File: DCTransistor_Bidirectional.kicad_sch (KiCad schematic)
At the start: 277 parts, among them J0 USB_C_Receptacle, Q0 MMBT3904, Q1 MMBT3904, Q2 AOD403, U0 CH340C, U2 ESP-12F, U3 SN74LVC1T45DBV, U4 TLV70233DBVR

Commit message: layout and footprint changes
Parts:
- removed SYMBOL0, SYMBOL1: ~, Jarrett_Footprint_Library:Trans_Symbol, symbol Jannett_Symbol_Library:Trans_Symbol
- removed SYMBOL2: ~, Jarrett_Footprint_Library:DCTransistor-Adjusted_Stations, symbol Jannett_Symbol_Library:Trans_Symbol
- added C48, C49: 0.1uF, Capacitor_SMD:C_0603_1608Metric, symbol Device:C_Small
- added H0, H1, H2, H3: MountingHole, MountingHole:MountingHole_6.4mm_M6, symbol Mechanical:MountingHole
- added TP0, TP1: 5016, jannett_footprints:TestPoint_Keystone_5016_Compact, symbol Connector:TestPoint
- D10, D100, D101, D102, D103, D104, D105, D106, D107, D108, D109, D11, D110, D111, D112, D113, D114, D115, D116, D117, D118, D119, D12, D120, D121, D122, D123, D124, D125, D126, D127, D128, D129, D13, D130, D131, D132, D133, D134, D135, D136, D137, D138, D139, D14, D140, D141, D142, D143, D144, D145, D146, D147, D148, D149, D15, D150, D151, D152, D153, D154, D155, D156, D157, D158, D159, D16, D160, D161, D162, D163, D164, D165, D166, D167, D168, D169, D17, D170, D171, D172, D173, D174, D175, D176, D177, D178, D179, D18, D180, D181, D182, D183, D184, D185, D186, D187, D188, D189, D19, D190, D191, D192, D193, D194, D195, D196, D197, D198, D199, D2, D20, D200, D201, D202, D203, D204, D205, D206, D207, D208, D21, D22, D23, D24, D25, D26, D27, D28, D29, D3, D30, D31, D32, D33, D34, D35, D36, D37, D38, D39, D4, D40, D41, D42, D43, D44, D45, D46, D47, D48, D49, D5, D50, D51, D52, D53, D54, D55, D56, D57, D58, D59, D6, D60, D61, D62, D63, D64, D65, D66, D67, D68, D69, D7, D70, D71, D72, D73, D74, D75, D76, D77, D78, D79, D8, D80, D81, D82, D83, D84, D85, D86, D87, D88, D89, D9, D90, D91, D92, D93, D94, D95, D96, D97, D98, D99: value WS2812B -> SKC6812RV; footprint LED_SMD:LED_WS2812B_PLCC4_5.0x5.0mm_P3.2mm -> jannett_footprints:LED_SK6812_PLCC4_5.0x5.0mm_P3.2mm_no_silk; symbol LED:WS2812B_2020_pinout -> LED:SK6812
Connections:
- net +3V3: now also C49.2
- net +5V: now also D10.3 (VDD), D100.3 (VDD), D101.3 (VDD), D102.3 (VDD), D103.3 (VDD), D104.3 (VDD), D105.3 (VDD), D106.3 (VDD), D107.3 (VDD), D108.3 (VDD), D109.3 (VDD), D11.3 (VDD), D110.3 (VDD), D111.3 (VDD), D112.3 (VDD), D113.3 (VDD), D114.3 (VDD), D115.3 (VDD), D116.3 (VDD), D117.3 (VDD), D118.3 (VDD), D119.3 (VDD), D12.3 (VDD), D120.3 (VDD), D121.3 (VDD), D122.3 (VDD), D123.3 (VDD), D124.3 (VDD), D125.3 (VDD), D126.3 (VDD), D127.3 (VDD), D128.3 (VDD), D129.3 (VDD), D13.3 (VDD), D130.3 (VDD), D131.3 (VDD), D132.3 (VDD), D133.3 (VDD), D134.3 (VDD), D135.3 (VDD), D136.3 (VDD), D137.3 (VDD), D138.3 (VDD), D139.3 (VDD), D14.3 (VDD), D140.3 (VDD), D141.3 (VDD), D142.3 (VDD), D143.3 (VDD), D144.3 (VDD), D145.3 (VDD), D146.3 (VDD), D147.3 (VDD), D148.3 (VDD), D149.3 (VDD), D15.3 (VDD), D150.3 (VDD), D151.3 (VDD), D152.3 (VDD), D153.3 (VDD), D154.3 (VDD), D155.3 (VDD), D156.3 (VDD), D157.3 (VDD), D158.3 (VDD), D159.3 (VDD), D16.3 (VDD), D160.3 (VDD), D161.3 (VDD), D162.3 (VDD), D163.3 (VDD), D164.3 (VDD), D165.3 (VDD), D166.3 (VDD), D167.3 (VDD), D168.3 (VDD), D169.3 (VDD), D17.3 (VDD), D170.3 (VDD), D171.3 (VDD), D172.3 (VDD), D173.3 (VDD), D174.3 (VDD), D175.3 (VDD), D176.3 (VDD), D177.3 (VDD), D178.3 (VDD), D179.3 (VDD), D18.3 (VDD), D180.3 (VDD), D181.3 (VDD), D182.3 (VDD), D183.3 (VDD), D184.3 (VDD), D185.3 (VDD), D186.3 (VDD), D187.3 (VDD), D188.3 (VDD), D189.3 (VDD), D19.3 (VDD), D190.3 (VDD), D191.3 (VDD), D192.3 (VDD), D193.3 (VDD), D194.3 (VDD), D195.3 (VDD), D196.3 (VDD), D197.3 (VDD), D198.3 (VDD), D199.3 (VDD), D2.3 (VDD), D20.3 (VDD), D200.3 (VDD), D201.3 (VDD), D202.3 (VDD), D203.3 (VDD), D204.3 (VDD), D205.3 (VDD), D206.3 (VDD), D207.3 (VDD), D208.3 (VDD), D21.3 (VDD), D22.3 (VDD), D23.3 (VDD), D24.3 (VDD), D25.3 (VDD), D26.3 (VDD), D27.3 (VDD), D28.3 (VDD), D29.3 (VDD), D3.3 (VDD), D30.3 (VDD), D31.3 (VDD), D32.3 (VDD), D33.3 (VDD), D34.3 (VDD), D35.3 (VDD), D36.3 (VDD), D37.3 (VDD), D38.3 (VDD), D39.3 (VDD), D4.3 (VDD), D40.3 (VDD), D41.3 (VDD), D42.3 (VDD), D43.3 (VDD), D44.3 (VDD), D45.3 (VDD), D46.3 (VDD), D47.3 (VDD), D48.3 (VDD), D49.3 (VDD), D5.3 (VDD), D50.3 (VDD), D51.3 (VDD), D52.3 (VDD), D53.3 (VDD), D54.3 (VDD), D55.3 (VDD), D56.3 (VDD), D57.3 (VDD), D58.3 (VDD), D59.3 (VDD), D6.3 (VDD), D60.3 (VDD), D61.3 (VDD), D62.3 (VDD), D63.3 (VDD), D64.3 (VDD), D65.3 (VDD), D66.3 (VDD), D67.3 (VDD), D68.3 (VDD), D69.3 (VDD), D7.3 (VDD), D70.3 (VDD), D71.3 (VDD), D72.3 (VDD), D73.3 (VDD), D74.3 (VDD), D75.3 (VDD), D76.3 (VDD), D77.3 (VDD), D78.3 (VDD), D79.3 (VDD), D8.3 (VDD), D80.3 (VDD), D81.3 (VDD), D82.3 (VDD), D83.3 (VDD), D84.3 (VDD), D85.3 (VDD), D86.3 (VDD), D87.3 (VDD), D88.3 (VDD), D89.3 (VDD), D9.3 (VDD), D90.3 (VDD), D91.3 (VDD), D92.3 (VDD), D93.3 (VDD), D94.3 (VDD), D95.3 (VDD), D96.3 (VDD), D97.3 (VDD), D98.3 (VDD), D99.3 (VDD), C48.1, TP0.1; no longer D10.4 (VDD), D100.4 (VDD), D101.4 (VDD), D102.4 (VDD), D103.4 (VDD), D104.4 (VDD), D105.4 (VDD), D106.4 (VDD), D107.4 (VDD), D108.4 (VDD), D109.4 (VDD), D11.4 (VDD), D110.4 (VDD), D111.4 (VDD), D112.4 (VDD), D113.4 (VDD), D114.4 (VDD), D115.4 (VDD), D116.4 (VDD), D117.4 (VDD), D118.4 (VDD), D119.4 (VDD), D12.4 (VDD), D120.4 (VDD), D121.4 (VDD), D122.4 (VDD), D123.4 (VDD), D124.4 (VDD), D125.4 (VDD), D126.4 (VDD), D127.4 (VDD), D128.4 (VDD), D129.4 (VDD), D13.4 (VDD), D130.4 (VDD), D131.4 (VDD), D132.4 (VDD), D133.4 (VDD), D134.4 (VDD), D135.4 (VDD), D136.4 (VDD), D137.4 (VDD), D138.4 (VDD), D139.4 (VDD), D14.4 (VDD), D140.4 (VDD), D141.4 (VDD), D142.4 (VDD), D143.4 (VDD), D144.4 (VDD), D145.4 (VDD), D146.4 (VDD), D147.4 (VDD), D148.4 (VDD), D149.4 (VDD), D15.4 (VDD), D150.4 (VDD), D151.4 (VDD), D152.4 (VDD), D153.4 (VDD), D154.4 (VDD), D155.4 (VDD), D156.4 (VDD), D157.4 (VDD), D158.4 (VDD), D159.4 (VDD), D16.4 (VDD), D160.4 (VDD), D161.4 (VDD), D162.4 (VDD), D163.4 (VDD), D164.4 (VDD), D165.4 (VDD), D166.4 (VDD), D167.4 (VDD), D168.4 (VDD), D169.4 (VDD), D17.4 (VDD), D170.4 (VDD), D171.4 (VDD), D172.4 (VDD), D173.4 (VDD), D174.4 (VDD), D175.4 (VDD), D176.4 (VDD), D177.4 (VDD), D178.4 (VDD), D179.4 (VDD), D18.4 (VDD), D180.4 (VDD), D181.4 (VDD), D182.4 (VDD), D183.4 (VDD), D184.4 (VDD), D185.4 (VDD), D186.4 (VDD), D187.4 (VDD), D188.4 (VDD), D189.4 (VDD), D19.4 (VDD), D190.4 (VDD), D191.4 (VDD), D192.4 (VDD), D193.4 (VDD), D194.4 (VDD), D195.4 (VDD), D196.4 (VDD), D197.4 (VDD), D198.4 (VDD), D199.4 (VDD), D2.4 (VDD), D20.4 (VDD), D200.4 (VDD), D201.4 (VDD), D202.4 (VDD), D203.4 (VDD), D204.4 (VDD), D205.4 (VDD), D206.4 (VDD), D207.4 (VDD), D208.4 (VDD), D21.4 (VDD), D22.4 (VDD), D23.4 (VDD), D24.4 (VDD), D25.4 (VDD), D26.4 (VDD), D27.4 (VDD), D28.4 (VDD), D29.4 (VDD), D3.4 (VDD), D30.4 (VDD), D31.4 (VDD), D32.4 (VDD), D33.4 (VDD), D34.4 (VDD), D35.4 (VDD), D36.4 (VDD), D37.4 (VDD), D38.4 (VDD), D39.4 (VDD), D4.4 (VDD), D40.4 (VDD), D41.4 (VDD), D42.4 (VDD), D43.4 (VDD), D44.4 (VDD), D45.4 (VDD), D46.4 (VDD), D47.4 (VDD), D48.4 (VDD), D49.4 (VDD), D5.4 (VDD), D50.4 (VDD), D51.4 (VDD), D52.4 (VDD), D53.4 (VDD), D54.4 (VDD), D55.4 (VDD), D56.4 (VDD), D57.4 (VDD), D58.4 (VDD), D59.4 (VDD), D6.4 (VDD), D60.4 (VDD), D61.4 (VDD), D62.4 (VDD), D63.4 (VDD), D64.4 (VDD), D65.4 (VDD), D66.4 (VDD), D67.4 (VDD), D68.4 (VDD), D69.4 (VDD), D7.4 (VDD), D70.4 (VDD), D71.4 (VDD), D72.4 (VDD), D73.4 (VDD), D74.4 (VDD), D75.4 (VDD), D76.4 (VDD), D77.4 (VDD), D78.4 (VDD), D79.4 (VDD), D8.4 (VDD), D80.4 (VDD), D81.4 (VDD), D82.4 (VDD), D83.4 (VDD), D84.4 (VDD), D85.4 (VDD), D86.4 (VDD), D87.4 (VDD), D88.4 (VDD), D89.4 (VDD), D9.4 (VDD), D90.4 (VDD), D91.4 (VDD), D92.4 (VDD), D93.4 (VDD), D94.4 (VDD), D95.4 (VDD), D96.4 (VDD), D97.4 (VDD), D98.4 (VDD), D99.4 (VDD)
- net 145-146: now also D145.4 (DOUT), D146.2 (DIN); no longer D145.1 (DOUT), D146.3 (DIN)
- net 73-74: now also D73.4 (DOUT), D74.2 (DIN); no longer D73.1 (DOUT), D74.3 (DIN)
- net DIN: now also D2.2 (DIN); no longer D2.3 (DIN)
- net GND: now also D10.1 (VSS), D100.1 (VSS), D101.1 (VSS), D102.1 (VSS), D103.1 (VSS), D104.1 (VSS), D105.1 (VSS), D106.1 (VSS), D107.1 (VSS), D108.1 (VSS), D109.1 (VSS), D11.1 (VSS), D110.1 (VSS), D111.1 (VSS), D112.1 (VSS), D113.1 (VSS), D114.1 (VSS), D115.1 (VSS), D116.1 (VSS), D117.1 (VSS), D118.1 (VSS), D119.1 (VSS), D12.1 (VSS), D120.1 (VSS), D121.1 (VSS), D122.1 (VSS), D123.1 (VSS), D124.1 (VSS), D125.1 (VSS), D126.1 (VSS), D127.1 (VSS), D128.1 (VSS), D129.1 (VSS), D13.1 (VSS), D130.1 (VSS), D131.1 (VSS), D132.1 (VSS), D133.1 (VSS), D134.1 (VSS), D135.1 (VSS), D136.1 (VSS), D137.1 (VSS), D138.1 (VSS), D139.1 (VSS), D14.1 (VSS), D140.1 (VSS), D141.1 (VSS), D142.1 (VSS), D143.1 (VSS), D144.1 (VSS), D145.1 (VSS), D146.1 (VSS), D147.1 (VSS), D148.1 (VSS), D149.1 (VSS), D15.1 (VSS), D150.1 (VSS), D151.1 (VSS), D152.1 (VSS), D153.1 (VSS), D154.1 (VSS), D155.1 (VSS), D156.1 (VSS), D157.1 (VSS), D158.1 (VSS), D159.1 (VSS), D16.1 (VSS), D160.1 (VSS), D161.1 (VSS), D162.1 (VSS), D163.1 (VSS), D164.1 (VSS), D165.1 (VSS), D166.1 (VSS), D167.1 (VSS), D168.1 (VSS), D169.1 (VSS), D17.1 (VSS), D170.1 (VSS), D171.1 (VSS), D172.1 (VSS), D173.1 (VSS), D174.1 (VSS), D175.1 (VSS), D176.1 (VSS), D177.1 (VSS), D178.1 (VSS), D179.1 (VSS), D18.1 (VSS), D180.1 (VSS), D181.1 (VSS), D182.1 (VSS), D183.1 (VSS), D184.1 (VSS), D185.1 (VSS), D186.1 (VSS), D187.1 (VSS), D188.1 (VSS), D189.1 (VSS), D19.1 (VSS), D190.1 (VSS), D191.1 (VSS), D192.1 (VSS), D193.1 (VSS), D194.1 (VSS), D195.1 (VSS), D196.1 (VSS), D197.1 (VSS), D198.1 (VSS), D199.1 (VSS), D2.1 (VSS), D20.1 (VSS), D200.1 (VSS), D201.1 (VSS), D202.1 (VSS), D203.1 (VSS), D204.1 (VSS), D205.1 (VSS), D206.1 (VSS), D207.1 (VSS), D208.1 (VSS), D21.1 (VSS), D22.1 (VSS), D23.1 (VSS), D24.1 (VSS), D25.1 (VSS), D26.1 (VSS), D27.1 (VSS), D28.1 (VSS), D29.1 (VSS), D3.1 (VSS), D30.1 (VSS), D31.1 (VSS), D32.1 (VSS), D33.1 (VSS), D34.1 (VSS), D35.1 (VSS), D36.1 (VSS), D37.1 (VSS), D38.1 (VSS), D39.1 (VSS), D4.1 (VSS), D40.1 (VSS), D41.1 (VSS), D42.1 (VSS), D43.1 (VSS), D44.1 (VSS), D45.1 (VSS), D46.1 (VSS), D47.1 (VSS), D48.1 (VSS), D49.1 (VSS), D5.1 (VSS), D50.1 (VSS), D51.1 (VSS), D52.1 (VSS), D53.1 (VSS), D54.1 (VSS), D55.1 (VSS), D56.1 (VSS), D57.1 (VSS), D58.1 (VSS), D59.1 (VSS), D6.1 (VSS), D60.1 (VSS), D61.1 (VSS), D62.1 (VSS), D63.1 (VSS), D64.1 (VSS), D65.1 (VSS), D66.1 (VSS), D67.1 (VSS), D68.1 (VSS), D69.1 (VSS), D7.1 (VSS), D70.1 (VSS), D71.1 (VSS), D72.1 (VSS), D73.1 (VSS), D74.1 (VSS), D75.1 (VSS), D76.1 (VSS), D77.1 (VSS), D78.1 (VSS), D79.1 (VSS), D8.1 (VSS), D80.1 (VSS), D81.1 (VSS), D82.1 (VSS), D83.1 (VSS), D84.1 (VSS), D85.1 (VSS), D86.1 (VSS), D87.1 (VSS), D88.1 (VSS), D89.1 (VSS), D9.1 (VSS), D90.1 (VSS), D91.1 (VSS), D92.1 (VSS), D93.1 (VSS), D94.1 (VSS), D95.1 (VSS), D96.1 (VSS), D97.1 (VSS), D98.1 (VSS), D99.1 (VSS), C48.2, C49.1, TP1.1; no longer D10.2 (VSS), D100.2 (VSS), D101.2 (VSS), D102.2 (VSS), D103.2 (VSS), D104.2 (VSS), D105.2 (VSS), D106.2 (VSS), D107.2 (VSS), D108.2 (VSS), D109.2 (VSS), D11.2 (VSS), D110.2 (VSS), D111.2 (VSS), D112.2 (VSS), D113.2 (VSS), D114.2 (VSS), D115.2 (VSS), D116.2 (VSS), D117.2 (VSS), D118.2 (VSS), D119.2 (VSS), D12.2 (VSS), D120.2 (VSS), D121.2 (VSS), D122.2 (VSS), D123.2 (VSS), D124.2 (VSS), D125.2 (VSS), D126.2 (VSS), D127.2 (VSS), D128.2 (VSS), D129.2 (VSS), D13.2 (VSS), D130.2 (VSS), D131.2 (VSS), D132.2 (VSS), D133.2 (VSS), D134.2 (VSS), D135.2 (VSS), D136.2 (VSS), D137.2 (VSS), D138.2 (VSS), D139.2 (VSS), D14.2 (VSS), D140.2 (VSS), D141.2 (VSS), D142.2 (VSS), D143.2 (VSS), D144.2 (VSS), D145.2 (VSS), D146.2 (VSS), D147.2 (VSS), D148.2 (VSS), D149.2 (VSS), D15.2 (VSS), D150.2 (VSS), D151.2 (VSS), D152.2 (VSS), D153.2 (VSS), D154.2 (VSS), D155.2 (VSS), D156.2 (VSS), D157.2 (VSS), D158.2 (VSS), D159.2 (VSS), D16.2 (VSS), D160.2 (VSS), D161.2 (VSS), D162.2 (VSS), D163.2 (VSS), D164.2 (VSS), D165.2 (VSS), D166.2 (VSS), D167.2 (VSS), D168.2 (VSS), D169.2 (VSS), D17.2 (VSS), D170.2 (VSS), D171.2 (VSS), D172.2 (VSS), D173.2 (VSS), D174.2 (VSS), D175.2 (VSS), D176.2 (VSS), D177.2 (VSS), D178.2 (VSS), D179.2 (VSS), D18.2 (VSS), D180.2 (VSS), D181.2 (VSS), D182.2 (VSS), D183.2 (VSS), D184.2 (VSS), D185.2 (VSS), D186.2 (VSS), D187.2 (VSS), D188.2 (VSS), D189.2 (VSS), D19.2 (VSS), D190.2 (VSS), D191.2 (VSS), D192.2 (VSS), D193.2 (VSS), D194.2 (VSS), D195.2 (VSS), D196.2 (VSS), D197.2 (VSS), D198.2 (VSS), D199.2 (VSS), D2.2 (VSS), D20.2 (VSS), D200.2 (VSS), D201.2 (VSS), D202.2 (VSS), D203.2 (VSS), D204.2 (VSS), D205.2 (VSS), D206.2 (VSS), D207.2 (VSS), D208.2 (VSS), D21.2 (VSS), D22.2 (VSS), D23.2 (VSS), D24.2 (VSS), D25.2 (VSS), D26.2 (VSS), D27.2 (VSS), D28.2 (VSS), D29.2 (VSS), D3.2 (VSS), D30.2 (VSS), D31.2 (VSS), D32.2 (VSS), D33.2 (VSS), D34.2 (VSS), D35.2 (VSS), D36.2 (VSS), D37.2 (VSS), D38.2 (VSS), D39.2 (VSS), D4.2 (VSS), D40.2 (VSS), D41.2 (VSS), D42.2 (VSS), D43.2 (VSS), D44.2 (VSS), D45.2 (VSS), D46.2 (VSS), D47.2 (VSS), D48.2 (VSS), D49.2 (VSS), D5.2 (VSS), D50.2 (VSS), D51.2 (VSS), D52.2 (VSS), D53.2 (VSS), D54.2 (VSS), D55.2 (VSS), D56.2 (VSS), D57.2 (VSS), D58.2 (VSS), D59.2 (VSS), D6.2 (VSS), D60.2 (VSS), D61.2 (VSS), D62.2 (VSS), D63.2 (VSS), D64.2 (VSS), D65.2 (VSS), D66.2 (VSS), D67.2 (VSS), D68.2 (VSS), D69.2 (VSS), D7.2 (VSS), D70.2 (VSS), D71.2 (VSS), D72.2 (VSS), D73.2 (VSS), D74.2 (VSS), D75.2 (VSS), D76.2 (VSS), D77.2 (VSS), D78.2 (VSS), D79.2 (VSS), D8.2 (VSS), D80.2 (VSS), D81.2 (VSS), D82.2 (VSS), D83.2 (VSS), D84.2 (VSS), D85.2 (VSS), D86.2 (VSS), D87.2 (VSS), D88.2 (VSS), D89.2 (VSS), D9.2 (VSS), D90.2 (VSS), D91.2 (VSS), D92.2 (VSS), D93.2 (VSS), D94.2 (VSS), D95.2 (VSS), D96.2 (VSS), D97.2 (VSS), D98.2 (VSS), D99.2 (VSS)
- new net: D132.4 (DOUT), D133.2 (DIN)
- new net: D133.4 (DOUT), D134.2 (DIN)
- new net: D91.4 (DOUT), D92.2 (DIN)
- new net: D92.4 (DOUT), D93.2 (DIN)
- new net: D140.4 (DOUT), D141.2 (DIN)
- new net: D141.4 (DOUT), D142.2 (DIN)
- new net: D56.4 (DOUT), D57.2 (DIN)
- new net: D57.4 (DOUT), D58.2 (DIN)
- new net: D11.4 (DOUT), D12.2 (DIN)
- new net: D12.4 (DOUT), D13.2 (DIN)
- new net: D81.4 (DOUT), D82.2 (DIN)
- new net: D82.4 (DOUT), D83.2 (DIN)
- new net: D146.4 (DOUT), D147.2 (DIN)
- new net: D147.4 (DOUT), D148.2 (DIN)
- new net: D165.4 (DOUT), D166.2 (DIN)
- new net: D166.4 (DOUT), D167.2 (DIN)
- new net: D94.4 (DOUT), D95.2 (DIN)
- new net: D95.4 (DOUT), D96.2 (DIN)
- new net: D167.4 (DOUT), D168.2 (DIN)
- new net: D168.4 (DOUT), D169.2 (DIN)
- new net: D68.4 (DOUT), D69.2 (DIN)
- new net: D69.4 (DOUT), D70.2 (DIN)
- new net: D183.4 (DOUT), D184.2 (DIN)
- new net: D184.4 (DOUT), D185.2 (DIN)
- new net: D182.4 (DOUT), D183.2 (DIN)
- new net: D139.4 (DOUT), D140.2 (DIN)
- new net: D176.4 (DOUT), D177.2 (DIN)
- new net: D177.4 (DOUT), D178.2 (DIN)
- new net: D202.4 (DOUT), D203.2 (DIN)
- new net: D203.4 (DOUT), D204.2 (DIN)
- new net: D152.4 (DOUT), D153.2 (DIN)
- new net: D153.4 (DOUT), D154.2 (DIN)
- new net: D20.4 (DOUT), D21.2 (DIN)
- new net: D21.4 (DOUT), D22.2 (DIN)
- new net: D195.4 (DOUT), D196.2 (DIN)
- new net: D196.4 (DOUT), D197.2 (DIN)
- new net: D26.4 (DOUT), D27.2 (DIN)
- new net: D27.4 (DOUT), D28.2 (DIN)
- new net: D106.4 (DOUT), D107.2 (DIN)
- new net: D107.4 (DOUT), D108.2 (DIN)
- new net: D200.4 (DOUT), D201.2 (DIN)
- new net: D201.4 (DOUT), D202.2 (DIN)
- new net: D115.4 (DOUT), D116.2 (DIN)
- new net: D116.4 (DOUT), D117.2 (DIN)
- new net: D104.4 (DOUT), D105.2 (DIN)
- new net: D105.4 (DOUT), D106.2 (DIN)
- new net: D83.4 (DOUT), D84.2 (DIN)
- new net: D93.4 (DOUT), D94.2 (DIN)
- new net: D151.4 (DOUT), D152.2 (DIN)
- new net: D117.4 (DOUT), D118.2 (DIN)
- new net: D118.4 (DOUT), D119.2 (DIN)
- new net: D179.4 (DOUT), D180.2 (DIN)
- new net: D180.4 (DOUT), D181.2 (DIN)
- new net: D127.4 (DOUT), D128.2 (DIN)
- new net: D128.4 (DOUT), D129.2 (DIN)
- new net: D45.4 (DOUT), D46.2 (DIN)
- new net: D46.4 (DOUT), D47.2 (DIN)
- new net: D67.4 (DOUT), D68.2 (DIN)
- new net: D7.4 (DOUT), D8.2 (DIN)
- new net: D8.4 (DOUT), D9.2 (DIN)
- new net: D16.4 (DOUT), D17.2 (DIN)
- new net: D17.4 (DOUT), D18.2 (DIN)
- new net: D98.4 (DOUT), D99.2 (DIN)
- new net: D100.2 (DIN), D99.4 (DOUT)
- new net: D77.4 (DOUT), D78.2 (DIN)
- new net: D78.4 (DOUT), D79.2 (DIN)
- new net: D54.4 (DOUT), D55.2 (DIN)
- new net: D55.4 (DOUT), D56.2 (DIN)
- new net: D150.4 (DOUT), D151.2 (DIN)
- new net: D103.4 (DOUT), D104.2 (DIN)
- new net: D126.4 (DOUT), D127.2 (DIN)
- new net: D188.4 (DOUT), D189.2 (DIN)
- new net: D189.4 (DOUT), D190.2 (DIN)
- new net: D101.4 (DOUT), D102.2 (DIN)
- new net: D102.4 (DOUT), D103.2 (DIN)
- new net: D48.4 (DOUT), D49.2 (DIN)
- new net: D49.4 (DOUT), D50.2 (DIN)
- new net: D53.4 (DOUT), D54.2 (DIN)
- new net: D28.4 (DOUT), D29.2 (DIN)
- new net: D66.4 (DOUT), D67.2 (DIN)
- new net: D114.4 (DOUT), D115.2 (DIN)
- new net: D169.4 (DOUT), D170.2 (DIN)
- new net: D175.4 (DOUT), D176.2 (DIN)
- new net: D90.4 (DOUT), D91.2 (DIN)
- new net: D18.4 (DOUT), D19.2 (DIN)
- new net: D19.4 (DOUT), D20.2 (DIN)
- new net: D112.4 (DOUT), D113.2 (DIN)
- new net: D113.4 (DOUT), D114.2 (DIN)
- new net: D100.4 (DOUT), D101.2 (DIN)
- new net: D71.4 (DOUT), D72.2 (DIN)
- new net: D72.4 (DOUT), D73.2 (DIN)
- new net: D24.4 (DOUT), D25.2 (DIN)
- new net: D25.4 (DOUT), D26.2 (DIN)
- new net: D158.4 (DOUT), D159.2 (DIN)
- new net: D159.4 (DOUT), D160.2 (DIN)
- new net: D173.4 (DOUT), D174.2 (DIN)
- new net: D174.4 (DOUT), D175.2 (DIN)
- new net: D142.4 (DOUT), D143.2 (DIN)
- new net: D143.4 (DOUT), D144.2 (DIN)
- new net: D88.4 (DOUT), D89.2 (DIN)
- new net: D89.4 (DOUT), D90.2 (DIN)
- new net: D197.4 (DOUT), D198.2 (DIN)
- new net: D163.4 (DOUT), D164.2 (DIN)
- new net: D164.4 (DOUT), D165.2 (DIN)
- new net: D186.4 (DOUT), D187.2 (DIN)
- new net: D187.4 (DOUT), D188.2 (DIN)
- new net: D111.4 (DOUT), D112.2 (DIN)
- new net: D162.4 (DOUT), D163.2 (DIN)
- new net: D37.4 (DOUT), D38.2 (DIN)
- new net: D38.4 (DOUT), D39.2 (DIN)
- new net: D35.4 (DOUT), D36.2 (DIN)
- new net: D36.4 (DOUT), D37.2 (DIN)
- new net: D5.4 (DOUT), D6.2 (DIN)
- new net: D6.4 (DOUT), D7.2 (DIN)
- new net: D129.4 (DOUT), D130.2 (DIN)
- new net: D84.4 (DOUT), D85.2 (DIN)
- new net: D85.4 (DOUT), D86.2 (DIN)
- new net: D32.4 (DOUT), D33.2 (DIN)
- new net: D33.4 (DOUT), D34.2 (DIN)
- new net: D191.4 (DOUT), D192.2 (DIN)
- new net: D192.4 (DOUT), D193.2 (DIN)
- new net: D13.4 (DOUT), D14.2 (DIN)
- new net: D14.4 (DOUT), D15.2 (DIN)
- new net: D47.4 (DOUT), D48.2 (DIN)
- new net: D155.4 (DOUT), D156.2 (DIN)
- new net: D156.4 (DOUT), D157.2 (DIN)
- new net: D30.4 (DOUT), D31.2 (DIN)
- new net: D31.4 (DOUT), D32.2 (DIN)
- new net: D44.4 (DOUT), D45.2 (DIN)
- new net: D86.4 (DOUT), D87.2 (DIN)
- new net: D87.4 (DOUT), D88.2 (DIN)
- new net: D15.4 (DOUT), D16.2 (DIN)
- new net: D144.4 (DOUT), D145.2 (DIN)
- new net: D62.4 (DOUT), D63.2 (DIN)
- new net: D63.4 (DOUT), D64.2 (DIN)
- new net: D122.4 (DOUT), D123.2 (DIN)
- new net: D123.4 (DOUT), D124.2 (DIN)
- new net: D23.4 (DOUT), D24.2 (DIN)
- new net: D193.4 (DOUT), D194.2 (DIN)
- new net: D64.4 (DOUT), D65.2 (DIN)
- new net: D52.4 (DOUT), D53.2 (DIN)
- new net: D43.4 (DOUT), D44.2 (DIN)
- new net: D170.4 (DOUT), D171.2 (DIN)
- new net: D154.4 (DOUT), D155.2 (DIN)
- new net: D124.4 (DOUT), D125.2 (DIN)
- new net: D125.4 (DOUT), D126.2 (DIN)
- new net: D108.4 (DOUT), D109.2 (DIN)
- new net: D51.4 (DOUT), D52.2 (DIN)
- new net: D204.4 (DOUT), D205.2 (DIN)
- new net: D149.4 (DOUT), D150.2 (DIN)
- new net: D185.4 (DOUT), D186.2 (DIN)
- new net: D130.4 (DOUT), D131.2 (DIN)
- new net: D131.4 (DOUT), D132.2 (DIN)
- new net: D110.4 (DOUT), D111.2 (DIN)
- new net: D178.4 (DOUT), D179.2 (DIN)
- new net: D198.4 (DOUT), D199.2 (DIN)
- new net: D199.4 (DOUT), D200.2 (DIN)
- new net: D34.4 (DOUT), D35.2 (DIN)
- new net: D190.4 (DOUT), D191.2 (DIN)
- new net: D160.4 (DOUT), D161.2 (DIN)
- new net: D79.4 (DOUT), D80.2 (DIN)
- new net: D80.4 (DOUT), D81.2 (DIN)
- new net: D96.4 (DOUT), D97.2 (DIN)
- new net: D97.4 (DOUT), D98.2 (DIN)
- new net: D61.4 (DOUT), D62.2 (DIN)
- new net: D70.4 (DOUT), D71.2 (DIN)
- new net: D50.4 (DOUT), D51.2 (DIN)
- new net: D109.4 (DOUT), D110.2 (DIN)
- new net: D2.4 (DOUT), D3.2 (DIN)
- new net: D59.4 (DOUT), D60.2 (DIN)
- new net: D60.4 (DOUT), D61.2 (DIN)
- new net: D65.4 (DOUT), D66.2 (DIN)
- new net: D76.4 (DOUT), D77.2 (DIN)
- new net: D74.4 (DOUT), D75.2 (DIN)
- new net: D75.4 (DOUT), D76.2 (DIN)
- new net: D10.4 (DOUT), D11.2 (DIN)
- new net: D205.4 (DOUT), D206.2 (DIN)
- new net: D161.4 (DOUT), D162.2 (DIN)
- new net: D29.4 (DOUT), D30.2 (DIN)
- new net: D207.4 (DOUT), D208.2 (DIN)
- new net: D4.4 (DOUT), D5.2 (DIN)
- new net: D39.4 (DOUT), D40.2 (DIN)
- new net: D40.4 (DOUT), D41.2 (DIN)
- new net: D194.4 (DOUT), D195.2 (DIN)
- new net: D157.4 (DOUT), D158.2 (DIN)
- new net: D136.4 (DOUT), D137.2 (DIN)
- new net: D137.4 (DOUT), D138.2 (DIN)
- new net: D148.4 (DOUT), D149.2 (DIN)
- new net: D22.4 (DOUT), D23.2 (DIN)
- new net: D121.4 (DOUT), D122.2 (DIN)
- new net: D41.4 (DOUT), D42.2 (DIN)
- new net: D42.4 (DOUT), D43.2 (DIN)
- new net: D138.4 (DOUT), D139.2 (DIN)
- new net: D120.4 (DOUT), D121.2 (DIN)
- new net: D206.4 (DOUT), D207.2 (DIN)
- new net: D181.4 (DOUT), D182.2 (DIN)
- new net: D3.4 (DOUT), D4.2 (DIN)
- new net: D119.4 (DOUT), D120.2 (DIN)
- new net: D10.2 (DIN), D9.4 (DOUT)
- new net: D58.4 (DOUT), D59.2 (DIN)
- new net: D135.4 (DOUT), D136.2 (DIN)
- new net: D134.4 (DOUT), D135.2 (DIN)
- new net: D171.4 (DOUT), D172.2 (DIN)
- new net: D172.4 (DOUT), D173.2 (DIN)

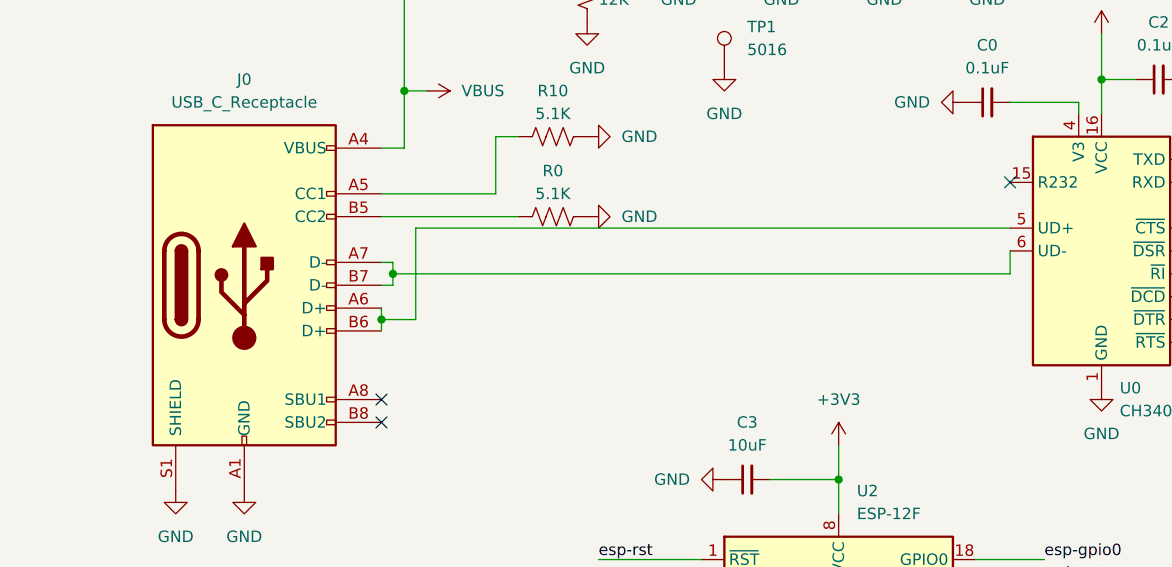
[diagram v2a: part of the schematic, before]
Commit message: layout fixes and schematic re-sync with layout
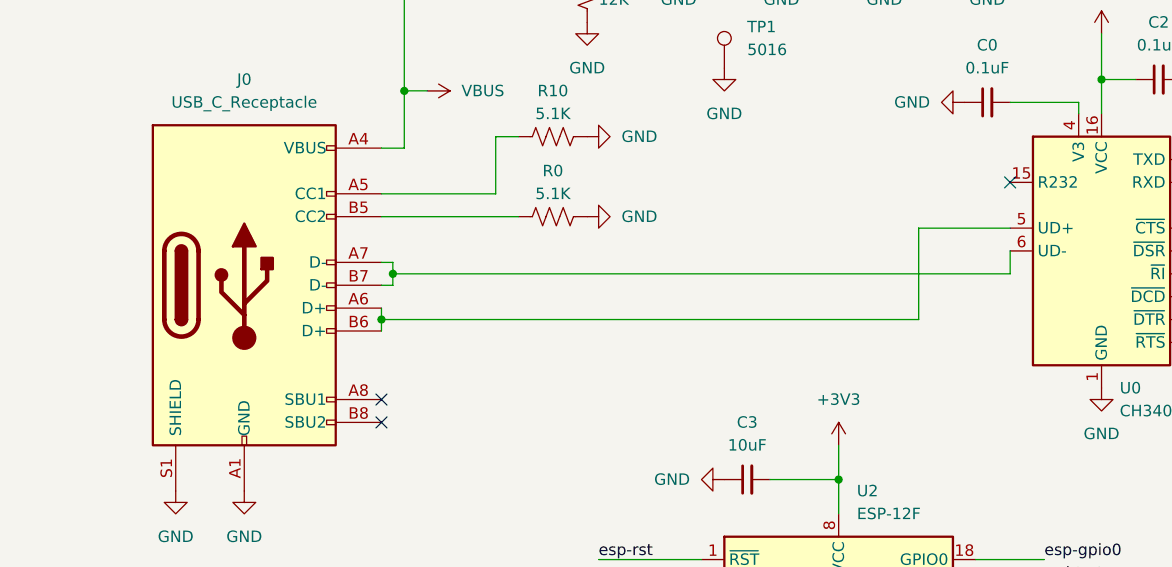
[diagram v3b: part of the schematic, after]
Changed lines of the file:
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@@
 (kicad_sch
-	(version 20231120)
+	(version 20250114)
 	(generator "eeschema")
-	(generator_version "8.0")
+	(generator_version "9.0")
 	(paper "D")
+	(text "All On:  42.61ma * 207 = 8.82A (not realistic, never would have all white)\n\nGreen: 14.08ma\nRed:    14.71ma * 207 = 3.04A (not realistic, never would be all full brightness and on)\nBlue:   14.28ma\n\nAll Off: 0.5ma\n"
+		(exclude_from_sim no)
+		(at 236.22 175.26 0)
+		(effects
+			(font
+				(size 1.27 1.27)
+			)
+			(justify left bottom)
+		)
+	)
+	(text "Jannett W"
+		(exclude_from_sim no)
+		(at 758.19 527.05 0)
+		(effects
+			(font
+				(face "Vivaldi")
+				(size 5 5)
+				(thickness 1)
+				(bold yes)
+			)
+			(justify left bottom)
+		)
+	)
 	(junction
 		(at 791.21 435.61)
@@
 	(wire
 		(pts
-			(xy 170.18 227.33) (xy 166.37 227.33)
+			(xy 226.06 227.33) (xy 166.37 227.33)
 		)
 		(stroke
@@
 	(wire
 		(pts
-			(xy 170.18 217.17) (xy 170.18 227.33)
+			(xy 226.06 217.17) (xy 226.06 227.33)
 		)
 		(stroke
@@
 	(wire
 		(pts
-			(xy 236.22 217.17) (xy 170.18 217.17)
+			(xy 236.22 217.17) (xy 226.06 217.17)
 		)
 		(stroke
@@
 		)
 	)
-	(text "All On:  42.61ma * 207 = 8.82A (not realistic, never would have all white)\n\nGreen: 14.08ma\nRed:    14.71ma * 207 = 3.04A (not realistic, never would be all full brightness and on)\nBlue:   14.28ma\n\nAll Off: 0.5ma\n"
-		(exclude_from_sim no)
-		(at 236.22 175.26 0)
-		(effects
-			(font
-				(size 1.27 1.27)
-			)
-			(justify left bottom)
-		)
-	)
-	(text "Jannett W"
-		(exclude_from_sim no)
-		(at 758.19 527.05 0)
-		(effects
-			(font
-				(face "Vivaldi")
-				(size 5 5)
-				(thickness 1)
-				(bold yes)
-			)
-			(justify left bottom)
-		)
-	)
 	(label "GND"
 		(at 1207.77 429.26 0)
@@
 		)
 	)
+	(embedded_fonts no)
 )

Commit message: layout updates
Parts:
- added TP2, TP3, TP4, TP5: 5016, jannett_footprints:TestPoint_Keystone_5016_Compact, symbol Connector:TestPoint
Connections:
- net +5V: now also TP4.1
- net DIN: now also TP2.1
- net GND: now also TP5.1
- net at D208.4 (DOUT): now also TP3.1
- no-connect marks 20 -> 19
